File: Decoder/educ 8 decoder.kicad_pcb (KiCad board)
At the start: 2 copper layers, 220 x 160 mm, 27 parts, among them J1 32-way-pcb-edge-Educ-8-connec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, J2 16-way-pcb-edge-Educ-8-connec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, U1 74LS00, U10 74LS00, U11 74LS00, U12 74LS00, U13 74LS00, U14 74LS04, U2 74LS10, U3 74LS04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

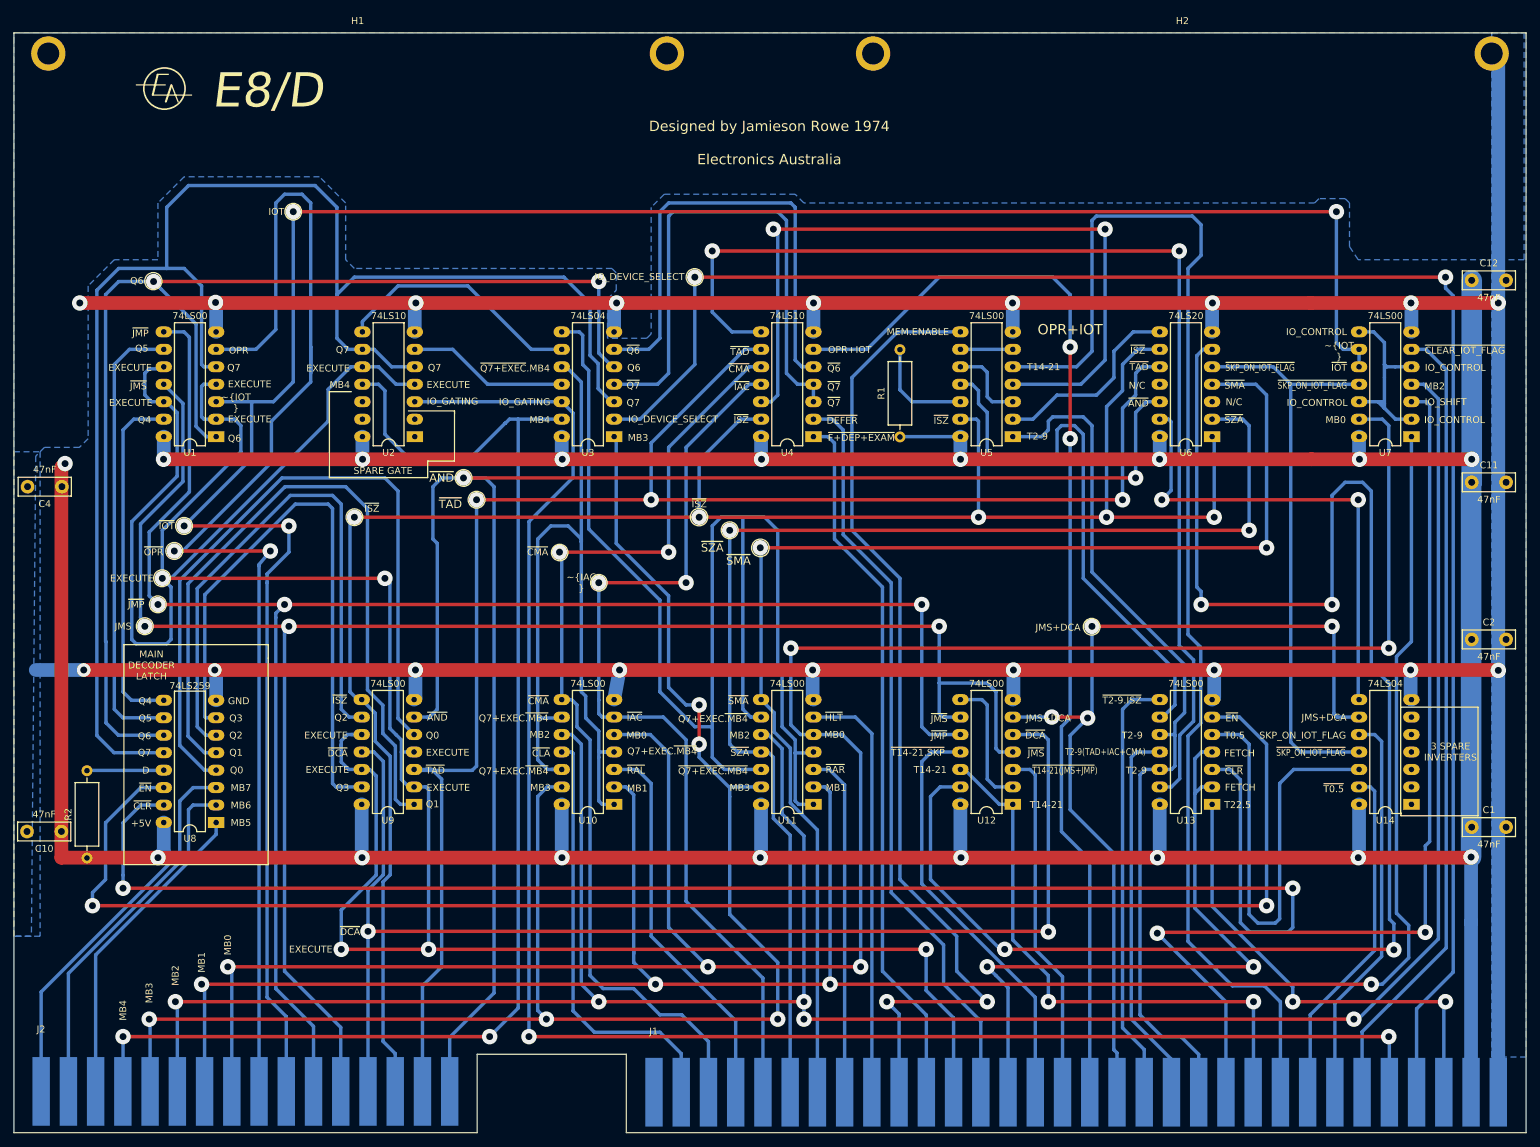
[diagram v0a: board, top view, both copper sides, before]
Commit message: Schematic update 2024-04-14 plus fixes
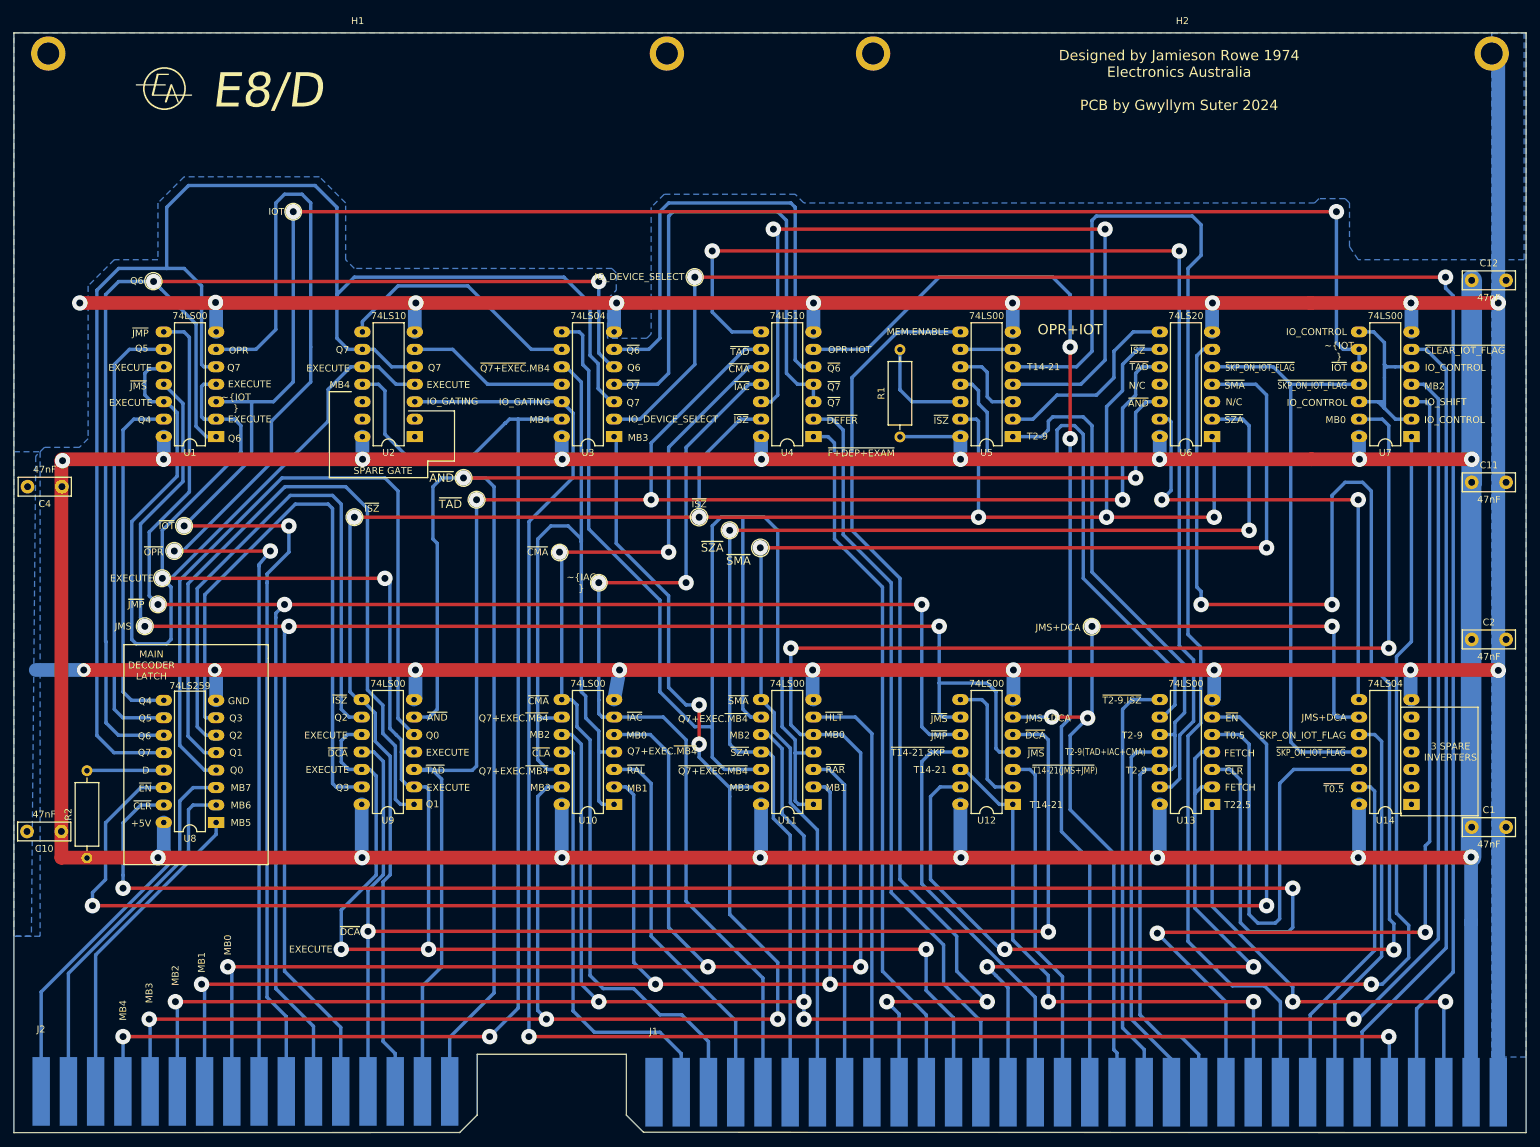
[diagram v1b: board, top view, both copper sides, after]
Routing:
- net +5V: track 656.2 -> 671.3 mm
- net ~{OPR}: track 191.0 -> 187.2 mm
- net /~{Q7+EXEC.}MB4: track 121.5 -> 118.5 mm
- net EXECUTE: track 398.1 -> 396.1 mm
- net ~{JMP}: track 255.1 -> 254.5 mm
- net MB1: track 334.0 -> 333.3 mm
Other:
- outline, holes or cut-outs redrawn
- board text added: "Designed by Jamieson Rowe 1974 Electronics Australia PCB by Gwyllym Suter 2024"
- board text removed: "Designed by Jamieson Rowe 1974 Electronics Australia"

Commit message: Changes 20-7-2025 E8/T. Connected 3 missing supply rail tracks to ICS Added flood fill top and bottom to reduce noise E8/F Corrected labelling on RHS board to reflect EXT_LA not GND Changed fast slow switch operation so fast is in the DOWN position. E8/C. Ran a new track to the 2 pin JST connector from EXT_LA from 10 pin connector on SR input. Added files for E8MX, 2k byte memory expansion board
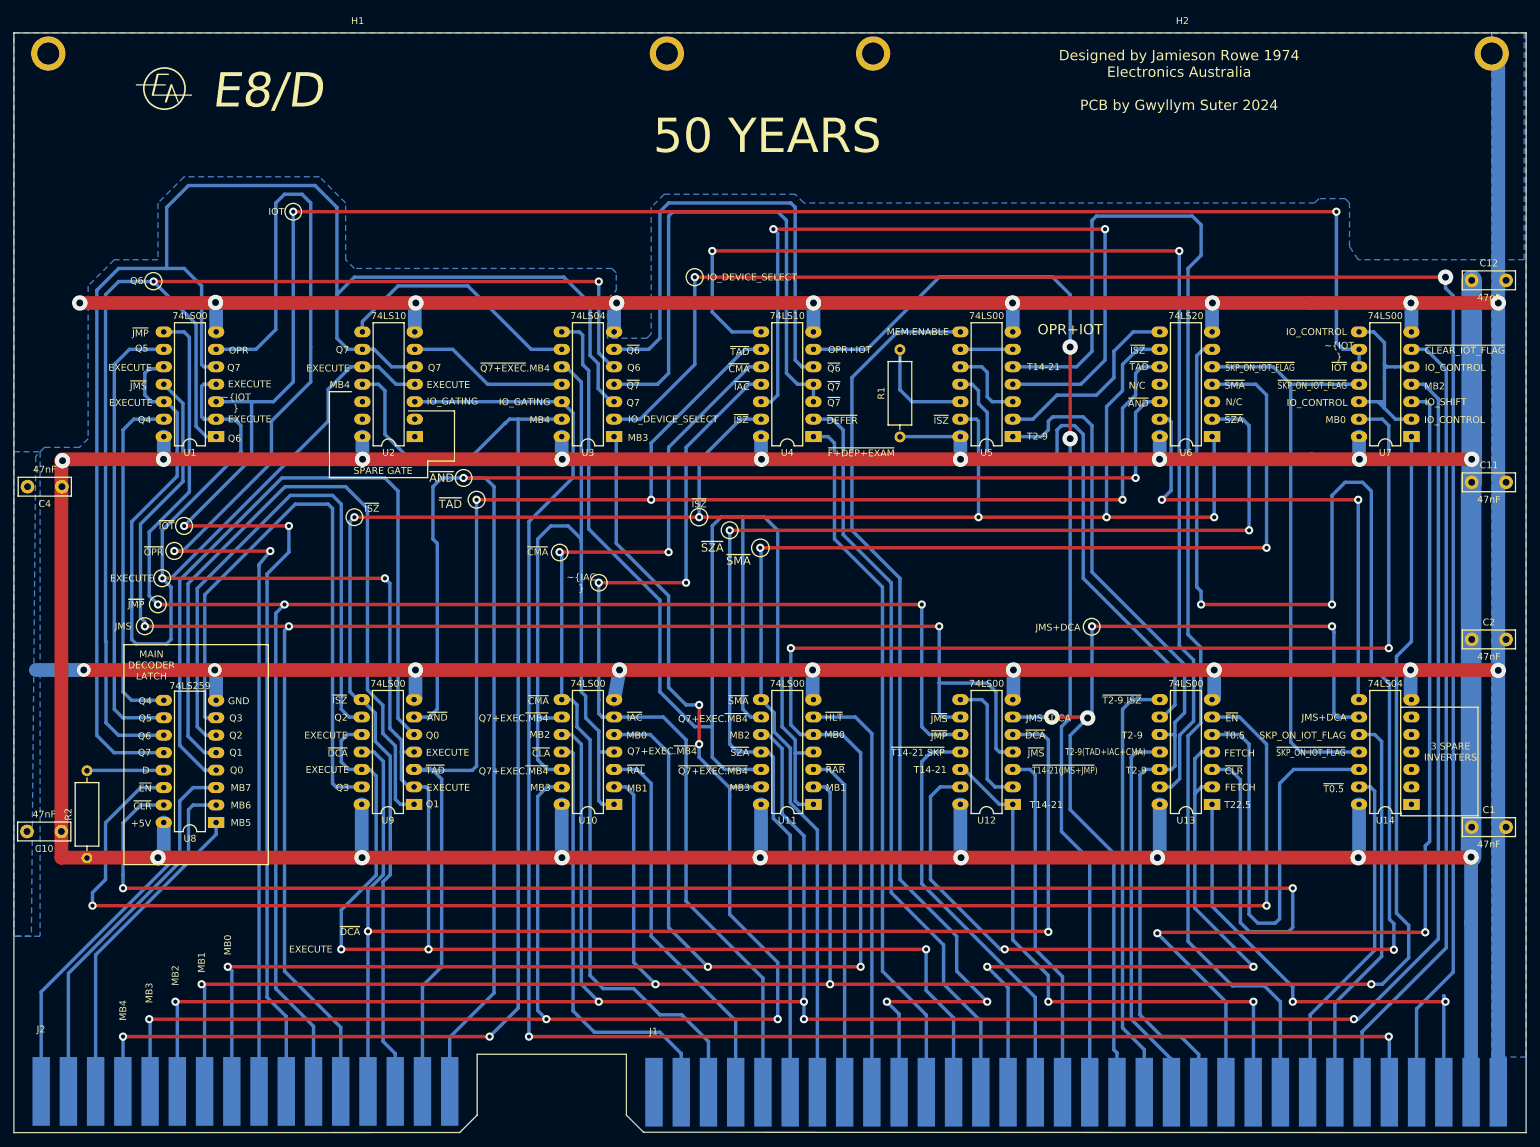
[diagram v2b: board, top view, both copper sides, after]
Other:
- board text added: "50 YEARS"
